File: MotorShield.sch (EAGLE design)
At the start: 119 parts, among them IC1 OPA4340E, IC2 OPA4340E, IC3 74HCT125D, X1 MSTBV2, X2 MSTBV8, X3 MSTBV8, X4 INPUTS, X5 BUTTON_LED, X6 DOTSTARS

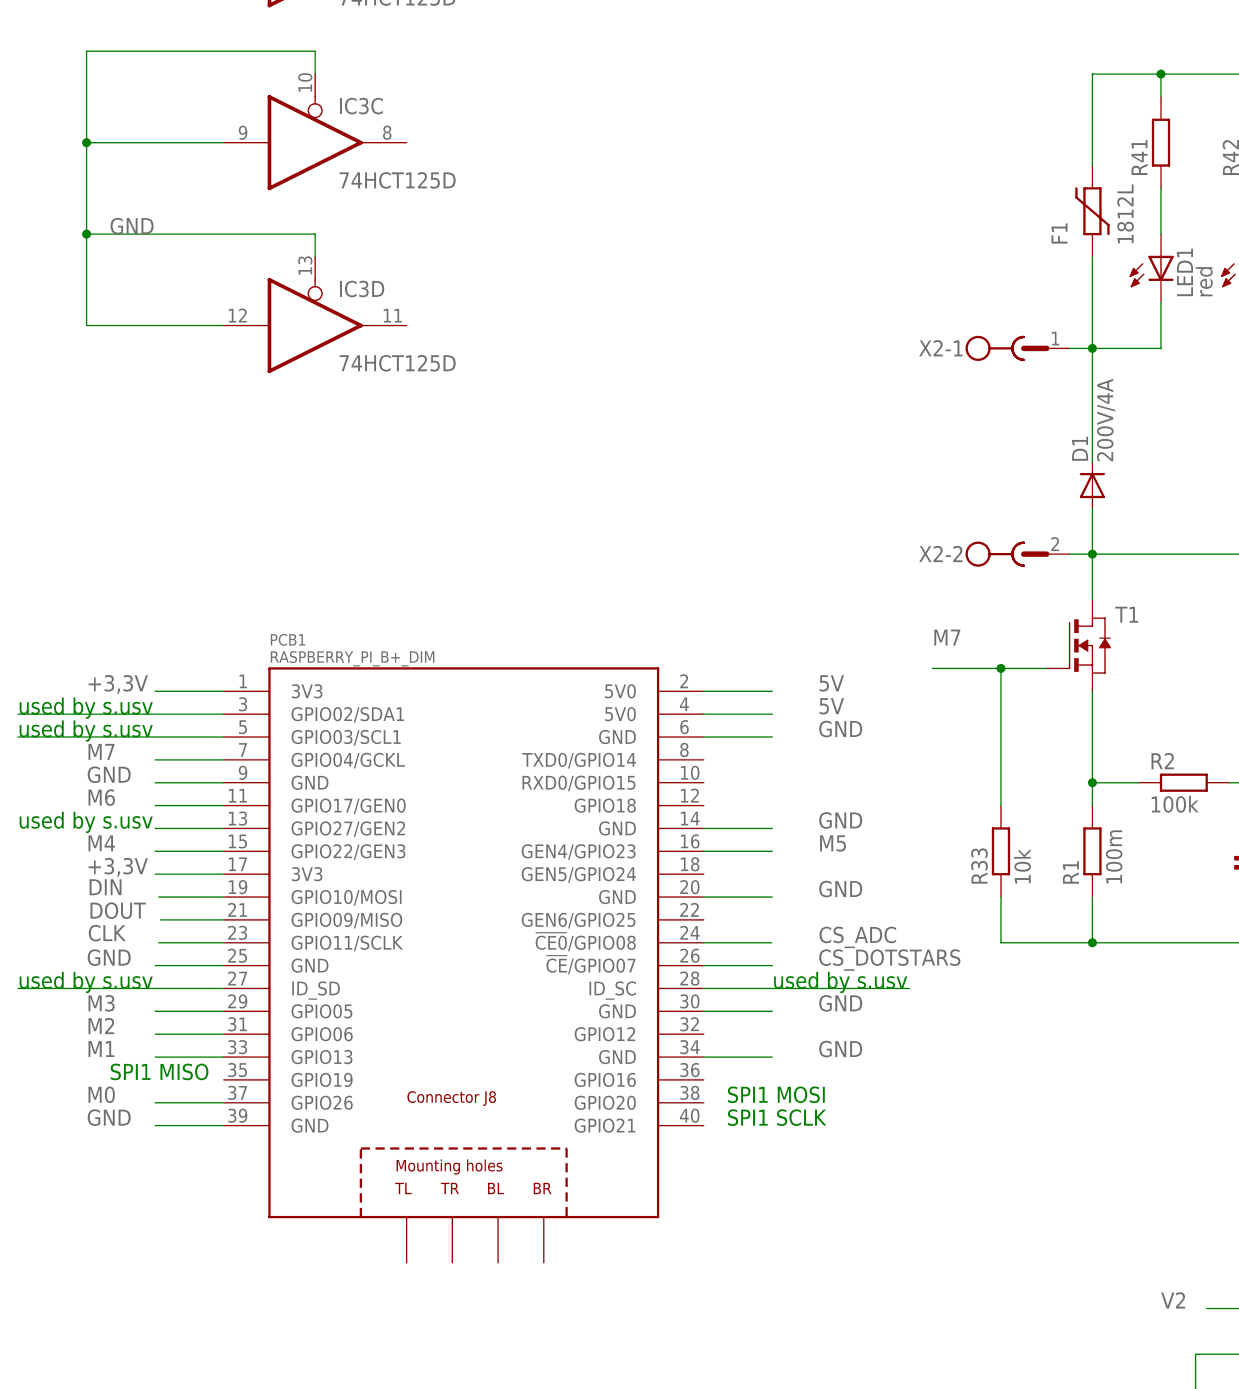
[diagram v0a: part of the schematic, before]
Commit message: added net classes and tried to place components for M1
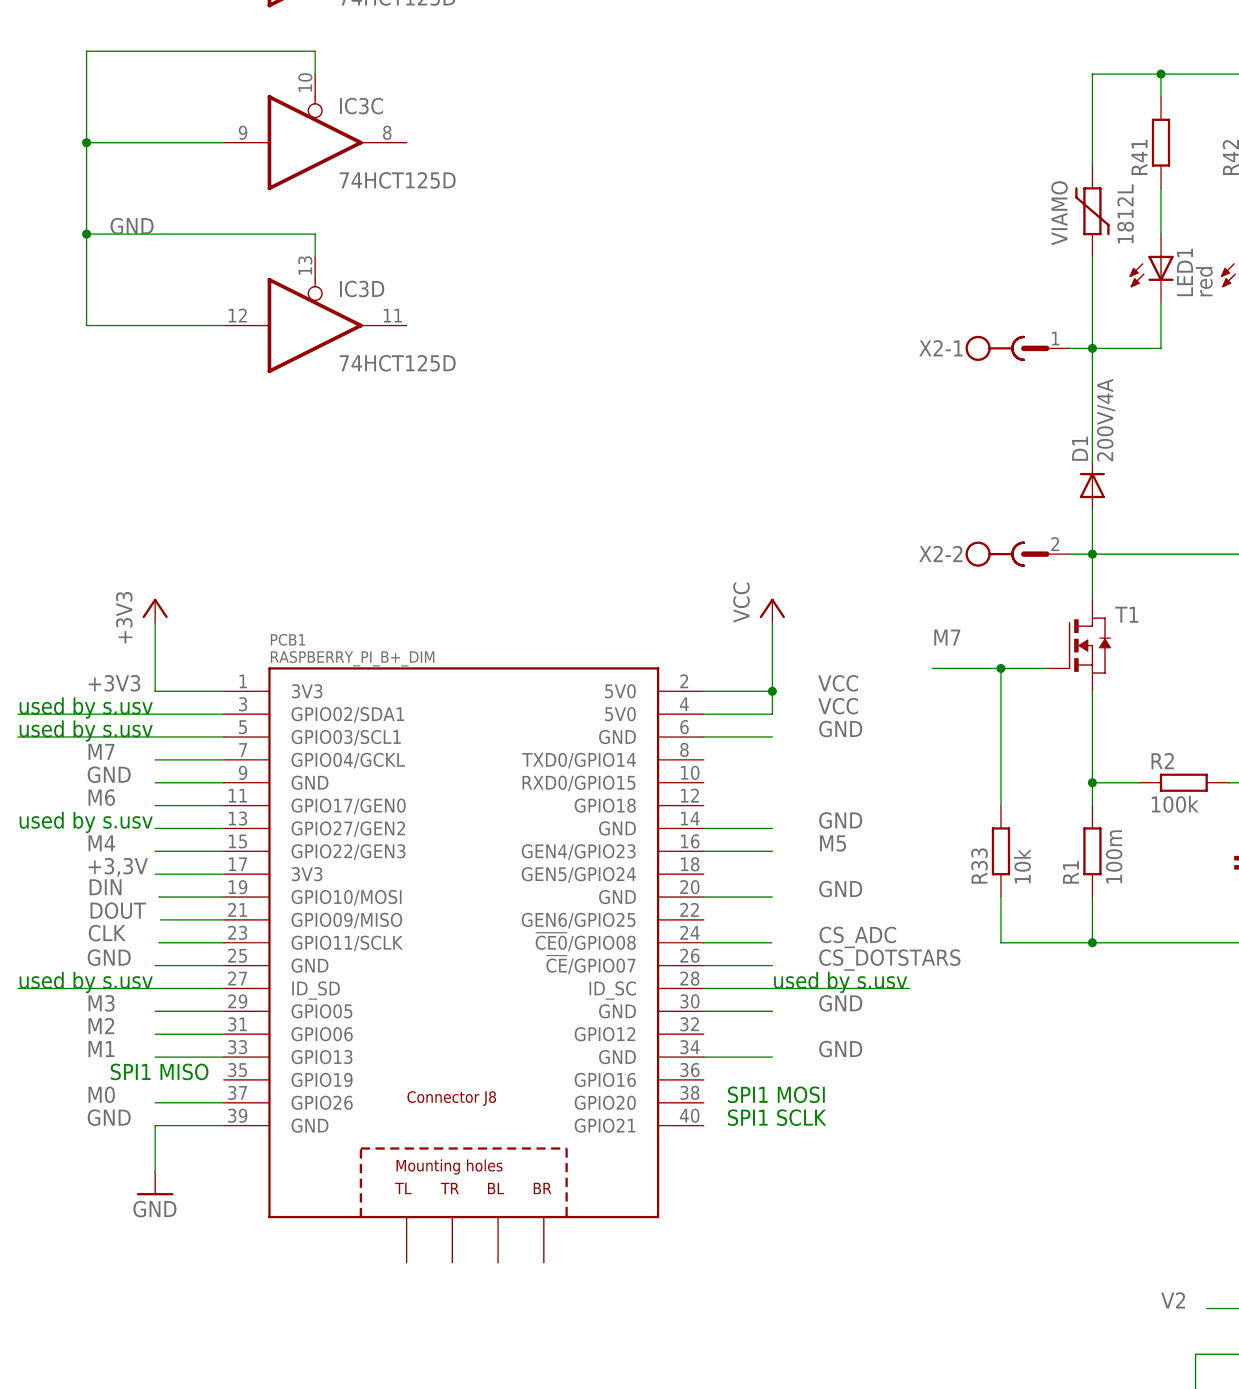
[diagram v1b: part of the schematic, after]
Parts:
- LED1, LED2: device led:LEDCHIP-LED0603 -> led:LEDCHIPLED_0603
- R1, R2: device rcl:R-EU_R0805 -> rcl:R-EU_R0603
- renumbered F1 to VIAMO
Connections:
- net 5V renamed VCC
- net +3,3V: no longer PCB1.3V3@1
- net +3V3: now also PCB1.3V3@1
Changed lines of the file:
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@@
 </variantdefs>
 <classes>
-<class number="0" name="default" width="0" drill="0">
+<class number="0" name="signal" width="0" drill="0">
+</class>
+<class number="1" name="motor 2A" width="0.4064" drill="0">
+</class>
+<class number="2" name="input 8A" width="2.54" drill="0">
 </class>
 </classes>
@@
 <part name="IC1" library="burr-brown" deviceset="OPA4340" device="E"/>
 <part name="IC2" library="burr-brown" deviceset="OPA4340" device="E"/>
-<part name="R1" library="rcl" deviceset="R-EU_" device="R0805" value="100m"/>
+<part name="R1" library="rcl" deviceset="R-EU_" device="R0603" value="100m"/>
 <part name="C1" library="eagle-ltspice" deviceset="C" device="" value="10nF"/>
 <part name="D1" library="diode" deviceset="DIODE-" device="DO214AA" value="200V/4A"/>
-<part name="R2" library="rcl" deviceset="R-EU_" device="R0805" value="100k"/>
+<part name="R2" library="rcl" deviceset="R-EU_" device="R0603" value="100k"/>
 <part name="R17" library="rcl" deviceset="R-EU_" device="R0805" value="27k"/>
 <part name="R18" library="rcl" deviceset="R-EU_" device="R0805" value="1k"/>
@@
 <part name="X6" library="con-wago255" deviceset="233-203" device="" value="DOTSTARS"/>
 <part name="GND4" library="supply1" deviceset="GND" device=""/>
-<part name="F1" library="ptc-littlefuse" deviceset="1812L" device=""/>
+<part name="VIAMO" library="ptc-littlefuse" deviceset="1812L" device=""/>
 <part name="F2" library="ptc-littlefuse" deviceset="1812L" device=""/>
 <part name="F3" library="ptc-littlefuse" deviceset="1812L" device=""/>
@@
 <part name="F7" library="ptc-littlefuse" deviceset="1812L" device=""/>
 <part name="F8" library="ptc-littlefuse" deviceset="1812L" device=""/>
-<part name="LED1" library="led" deviceset="LED" device="CHIP-LED0603" value="red"/>
-<part name="LED2" library="led" deviceset="LED" device="CHIP-LED0603" value="yellow"/>
+<part name="LED1" library="led" deviceset="LED" device="CHIPLED_0603" value="red"/>
+<part name="LED2" library="led" deviceset="LED" device="CHIPLED_0603" value="yellow"/>
 <part name="LED3" library="led" deviceset="LED" device="CHIP-LED0603" value="red"/>
 <part name="LED4" library="led" deviceset="LED" device="CHIP-LED0603" value="yellow"/>
@@
 <part name="+3V1" library="supply1" deviceset="+3V3" device=""/>
 <part name="C9" library="rcl" deviceset="C-EU" device="C0805" value="100nF"/>
+<part name="P+4" library="supply1" deviceset="VCC" device=""/>
+<part name="GND7" library="supply1" deviceset="GND" device=""/>
+<part name="+3V2" library="supply1" deviceset="+3V3" device=""/>
 </parts>
 <sheets>
@@
 <instance part="X6" gate="G$1" x="60.96" y="187.96"/>
 <instance part="GND4" gate="1" x="48.26" y="175.26"/>
-<instance part="F1" gate="G$1" x="91.44" y="139.7" rot="R90"/>
+<instance part="VIAMO" gate="G$1" x="91.44" y="139.7" rot="R90"/>
 <instance part="F2" gate="G$1" x="132.08" y="139.7" rot="R90"/>
 <instance part="F3" gate="G$1" x="172.72" y="139.7" rot="R90"/>
@@
 <instance part="+3V1" gate="G$1" x="335.28" y="27.94"/>
 <instance part="C9" gate="G$1" x="342.9" y="17.78"/>
+<instance part="P+4" gate="VCC" x="55.88" y="96.52"/>
+<instance part="GND7" gate="1" x="-12.7" y="30.48"/>
+<instance part="+3V2" gate="G$1" x="-12.7" y="96.52"/>
 </instances>
 <busses>
@@
 </segment>
 </net>
-<net name="GND" class="0">
+<net name="GND" class="1">
 <segment>
 <pinref part="IC1" gate="A" pin="V-"/>
@@
 <wire x1="-5.08" y1="38.1" x2="-12.7" y2="38.1" width="0.1524" layer="91"/>
 <label x="-20.32" y="38.1" size="1.778" layer="95"/>
+<pinref part="GND7" gate="1" pin="GND"/>
+<wire x1="-12.7" y1="33.02" x2="-12.7" y2="38.1" width="0.1524" layer="91"/>
 </segment>
 <segment>
@@
 </segment>
 <segment>
-<pinref part="PCB1" gate="G$1" pin="3V3@1"/>
-<wire x1="-5.08" y1="86.36" x2="-12.7" y2="86.36" width="0.1524" layer="91"/>
-<label x="-20.32" y="86.36" size="1.778" layer="95"/>
-</segment>
-<segment>
 <pinref part="PCB1" gate="G$1" pin="3V3@2"/>
 <wire x1="-5.08" y1="66.04" x2="-12.7" y2="66.04" width="0.1524" layer="91"/>
@@
 </segment>
 </net>
-<net name="5V" class="0">
-<segment>
-<pinref part="PCB1" gate="G$1" pin="5V0@1"/>
-<wire x1="48.26" y1="86.36" x2="55.88" y2="86.36" width="0.1524" layer="91"/>
-<label x="60.96" y="86.36" size="1.778" layer="95"/>
-</segment>
-<segment>
-<pinref part="PCB1" gate="G$1" pin="5V0@2"/>
-<wire x1="48.26" y1="83.82" x2="55.88" y2="83.82" width="0.1524" layer="91"/>
-<label x="60.96" y="83.82" size="1.778" layer="95"/>
-</segment>
-</net>
-<net name="N$2" class="0">
+<net name="N$2" class="1">
 <segment>
 <pinref part="D1" gate="G$1" pin="A"/>
@@
 </segment>
 </net>
-<net name="N$3" class="0">
+<net name="N$3" class="1">
 <segment>
 <pinref part="R1" gate="G$1" pin="2"/>
@@
 </segment>
 </net>
-<net name="N$10" class="0">
+<net name="N$10" class="1">
 <segment>
 <pinref part="D2" gate="G$1" pin="A"/>
@@
 </segment>
 </net>
-<net name="N$11" class="0">
+<net name="N$11" class="1">
 <segment>
 <pinref part="R3" gate="G$1" pin="2"/>
@@
 </segment>
 </net>
-<net name="N$17" class="0">
+<net name="N$17" class="1">
 <segment>
 <pinref part="D3" gate="G$1" pin="A"/>
@@
 </segment>
 </net>
-<net name="N$18" class="0">
+<net name="N$18" class="1">
 <segment>
 <pinref part="R6" gate="G$1" pin="2"/>
@@
 </segment>
 </net>
-<net name="N$26" class="0">
+<net name="N$26" class="1">
 <segment>
 <pinref part="D4" gate="G$1" pin="A"/>
@@
 </segment>
 </net>
-<net name="N$29" class="0">
+<net name="N$29" class="1">
 <segment>
 <pinref part="R9" gate="G$1" pin="2"/>
@@
 </segment>
 </net>
-<net name="N$38" class="0">
+<net name="N$38" class="1">
 <segment>
 <pinref part="D5" gate="G$1" pin="A"/>
@@
 </segment>
 </net>
-<net name="N$39" class="0">
+<net name="N$39" class="1">
 <segment>
 <pinref part="R12" gate="G$1" pin="2"/>
@@
 </segment>
 </net>
-<net name="N$45" class="0">
+<net name="N$45" class="1">
 <segment>
 <pinref part="D6" gate="G$1" pin="A"/>
@@
 </segment>
 </net>
-<net name="N$46" class="0">
+<net name="N$46" class="1">
 <segment>
 <pinref part="R15" gate="G$1" pin="2"/>
@@
 </segment>
 </net>
-<net name="N$51" class="0">
+<net name="N$51" class="1">
 <segment>
 <pinref part="D7" gate="G$1" pin="A"/>
@@
 </segment>
 </net>
-<net name="N$52" class="0">
+<net name="N$52" class="1">
 <segment>
 <pinref part="R35" gate="G$1" pin="2"/>
@@
 </segment>
 </net>
-<net name="24V/1A" class="0">
+<net name="24V/1A" class="1">
 <segment>
 <pinref part="D1" gate="G$1" pin="C"/>
@@
 <junction x="91.44" y="124.46"/>
 <pinref part="X2" gate="-1" pin="1"/>
-<pinref part="F1" gate="G$1" pin="1"/>
+<pinref part="VIAMO" gate="G$1" pin="1"/>
 <pinref part="LED1" gate="G$1" pin="C"/>
 <wire x1="91.44" y1="124.46" x2="99.06" y2="124.46" width="0.1524" layer="91"/>
@@
 </segment>
 </net>
-<net name="N$57" class="0">
+<net name="N$57" class="1">
 <segment>
 <pinref part="D8" gate="G$1" pin="A"/>
@@
 </segment>
 </net>
-<net name="N$58" class="0">
+<net name="N$58" class="1">
 <segment>
 <pinref part="R38" gate="G$1" pin="2"/>
@@
 </segment>
 </net>
-<net name="N$4" class="0">
+<net name="N$4" class="1">
 <segment>
 <pinref part="D8" gate="G$1" pin="C"/>
@@
 </segment>
 </net>
-<net name="N$5" class="0">
+<net name="N$5" class="1">
 <segment>
 <pinref part="D7" gate="G$1" pin="C"/>
@@
 </segment>
 </net>
-<net name="N$7" class="0">
+<net name="N$7" class="1">
 <segment>
 <pinref part="D6" gate="G$1" pin="C"/>
@@
 </segment>
 </net>
-<net name="N$8" class="0">
+<net name="N$8" class="1">
 <segment>
 <pinref part="D5" gate="G$1" pin="C"/>
@@
 </segment>
 </net>
-<net name="N$9" class="0">
+<net name="N$9" class="1">
 <segment>
 <pinref part="D4" gate="G$1" pin="C"/>
@@
 </segment>
 </net>
-<net name="N$12" class="0">
+<net name="N$12" class="1">
 <segment>
 <pinref part="D3" gate="G$1" pin="C"/>
@@
 </segment>
 </net>
-<net name="N$13" class="0">
+<net name="N$13" class="1">
 <segment>
 <pinref part="D2" gate="G$1" pin="C"/>
@@
 </segment>
 </net>
-<net name="N$23" class="0">
+<net name="N$23" class="2">
 <segment>
 <pinref part="X1" gate="-1" pin="1"/>
@@
 </segment>
 </net>
-<net name="+24V" class="0">
+<net name="+24V" class="1">
 <segment>
 <pinref part="P+2" gate="1" pin="+24V"/>
@@
 <pinref part="F3" gate="G$1" pin="2"/>
 <pinref part="F2" gate="G$1" pin="2"/>
-<pinref part="F1" gate="G$1" pin="2"/>
+<pinref part="VIAMO" gate="G$1" pin="2"/>
 <pinref part="P+3" gate="1" pin="+24V"/>
 <wire x1="375.92" y1="162.56" x2="375.92" y2="154.94" width="0.1524" layer="91"/>
@@
 <junction x="335.28" y="22.86"/>
 </segment>
-</net>
+<segment>
+<pinref part="PCB1" gate="G$1" pin="3V3@1"/>
+<wire x1="-5.08" y1="86.36" x2="-12.7" y2="86.36" width="0.1524" layer="91"/>
+<label x="-20.32" y="86.36" size="1.778" layer="95"/>
+<pinref part="+3V2" gate="G$1" pin="+3V3"/>
+<wire x1="-12.7" y1="86.36" x2="-12.7" y2="93.98" width="0.1524" layer="91"/>
+</segment>
+</net>
+<net name="VCC" class="0">
+<segment>
+<pinref part="PCB1" gate="G$1" pin="5V0@1"/>
+<wire x1="48.26" y1="86.36" x2="55.88" y2="86.36" width="0.1524" layer="91"/>
+<label x="60.96" y="86.36" size="1.778" layer="95"/>
+<pinref part="P+4" gate="VCC" pin="VCC"/>
+<wire x1="55.88" y1="93.98" x2="55.88" y2="86.36" width="0.1524" layer="91"/>
+<pinref part="PCB1" gate="G$1" pin="5V0@2"/>
+<wire x1="48.26" y1="83.82" x2="55.88" y2="83.82" width="0.1524" layer="91"/>
+<label x="60.96" y="83.82" size="1.778" layer="95"/>
+<wire x1="55.88" y1="86.36" x2="55.88" y2="83.82" width="0.1524" layer="91"/>
+<junction x="55.88" y="86.36"/>
+</segment>
+</net>
